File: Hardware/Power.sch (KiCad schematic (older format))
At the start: 20 parts, among them U8 AOZ1280

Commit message: Clear annotations
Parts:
- renumbered C39 to C?, C41 to C?, C44 to C?, D36 to D?, L2 to L?, R37 to R?, R38 to R?, R34 to R?, SH1 to SH?, SH2 to SH?, SH3 to SH?, SH4 to SH?, U8 to U?
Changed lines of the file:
@@
 $EndDescr
 $Comp
-L +3.3V #PWR099
+L +3.3V #PWR?
 U 1 1 5241F48B
 P 5300 4800
-F 0 "#PWR099" H 5300 4760 30  0001 C CNN
+F 0 "#PWR?" H 5300 4760 30  0001 C CNN
 F 1 "+3.3V" H 5300 4910 30  0000 C CNN
 F 2 "" H 5300 4800 60  0000 C CNN
@@
 $EndComp
 $Comp
-L AOZ1280 U8
+L AOZ1280 U?
 U 1 1 52455ED9
 P 3550 5250
-F 0 "U8" H 3550 4800 60  0000 C CNN
+F 0 "U?" H 3550 4800 60  0000 C CNN
 F 1 "AOZ1280" V 3550 5250 60  0000 C CNN
 F 2 "" H 3550 5600 60  0000 C CNN
@@
 $EndComp
 $Comp
-L DIODE-SCH D36
+L DIODE-SCH D?
 U 1 1 52455EF2
 P 4100 5250
-F 0 "D36" H 4100 5350 60  0000 C CNN
+F 0 "D?" H 4100 5350 60  0000 C CNN
 F 1 "CDBA140" H 4100 5150 60  0000 C CNN
 F 2 "~" H 4100 5250 60  0000 C CNN
@@
 $EndComp
 $Comp
-L R R37
+L R R?
 U 1 1 52455F0B
 P 4800 5250
-F 0 "R37" H 4800 5350 50  0000 C CNN
+F 0 "R?" H 4800 5350 50  0000 C CNN
 F 1 "49.9k" H 4800 5250 50  0000 C CNN
 F 2 "RESC1608" H 4800 5250 60  0001 C CNN
@@
 $EndComp
 $Comp
-L R R38
+L R R?
 U 1 1 52455F41
 P 4800 5950
-F 0 "R38" H 4800 6050 50  0000 C CNN
+F 0 "R?" H 4800 6050 50  0000 C CNN
 F 1 "15.8k" H 4800 5950 50  0000 C CNN
 F 2 "RESC1608" H 4800 5950 60  0001 C CNN
@@
 $EndComp
 $Comp
-L GND #PWR0106
+L GND #PWR?
 U 1 1 5245631B
 P 2400 5800
-F 0 "#PWR0106" H 2400 5800 30  0001 C CNN
+F 0 "#PWR?" H 2400 5800 30  0001 C CNN
 F 1 "GND" H 2400 5730 30  0001 C CNN
 F 2 "" H 2400 5800 60  0000 C CNN
@@
 $EndComp
 $Comp
-L GND #PWR0107
+L GND #PWR?
 U 1 1 5245632A
 P 3000 5700
-F 0 "#PWR0107" H 3000 5700 30  0001 C CNN
+F 0 "#PWR?" H 3000 5700 30  0001 C CNN
 F 1 "GND" H 3000 5630 30  0001 C CNN
 F 2 "" H 3000 5700 60  0000 C CNN
@@
 $EndComp
 $Comp
-L GND #PWR0108
+L GND #PWR?
 U 1 1 52456339
 P 5300 5600
-F 0 "#PWR0108" H 5300 5600 30  0001 C CNN
+F 0 "#PWR?" H 5300 5600 30  0001 C CNN
 F 1 "GND" H 5300 5530 30  0001 C CNN
 F 2 "" H 5300 5600 60  0000 C CNN
@@
 $EndComp
 $Comp
-L GND #PWR0109
+L GND #PWR?
 U 1 1 52456348
 P 4800 6300
-F 0 "#PWR0109" H 4800 6300 30  0001 C CNN
+F 0 "#PWR?" H 4800 6300 30  0001 C CNN
 F 1 "GND" H 4800 6230 30  0001 C CNN
 F 2 "" H 4800 6300 60  0000 C CNN
@@
 $EndComp
 $Comp
-L GND #PWR0110
+L GND #PWR?
 U 1 1 52456357
 P 4100 5700
-F 0 "#PWR0110" H 4100 5700 30  0001 C CNN
+F 0 "#PWR?" H 4100 5700 30  0001 C CNN
 F 1 "GND" H 4100 5630 30  0001 C CNN
 F 2 "" H 4100 5700 60  0000 C CNN
@@
 $EndComp
 $Comp
-L L L2
+L L L?
 U 1 1 524569D1
 P 4450 4900
-F 0 "L2" H 4450 4800 60  0000 C CNN
+F 0 "L?" H 4450 4800 60  0000 C CNN
 F 1 "10uH" H 4450 4950 60  0000 C CNN
 F 2 "INDC3225" H 4450 4900 60  0001 C CNN
@@
 $EndComp
 $Comp
-L C C39
+L C C?
 U 1 1 52456A9F
 P 2400 5450
-F 0 "C39" H 2450 5600 60  0000 L CNN
+F 0 "C?" H 2450 5600 60  0000 L CNN
 F 1 "10uF" H 2450 5300 60  0000 L CNN
 F 2 "~" H 2400 5450 60  0000 C CNN
@@
 Lx
 $Comp
-L C C41
+L C C?
 U 1 1 52457190
 P 3550 4500
-F 0 "C41" H 3600 4650 60  0000 L CNN
+F 0 "C?" H 3600 4650 60  0000 L CNN
 F 1 "0.01uF" H 3600 4350 60  0000 L CNN
 F 2 "CAPC1608" H 3550 4500 60  0001 C CNN
@@
 $EndComp
 $Comp
-L C C44
+L C C?
 U 1 1 5245816D
 P 5300 5250
-F 0 "C44" H 5350 5400 60  0000 L CNN
+F 0 "C?" H 5350 5400 60  0000 L CNN
 F 1 "10uF" H 5350 5100 60  0000 L CNN
 F 2 "~" H 5300 5250 60  0000 C CNN
@@
 Bst
 $Comp
-L TP SH1
+L TP SH?
 U 1 1 52BCE4A7
 P 7600 3400
-F 0 "SH1" H 7600 3750 60  0000 C CNN
+F 0 "SH?" H 7600 3750 60  0000 C CNN
 F 1 "SHIELD" H 7600 3650 60  0000 C CNN
 F 2 "EMI-TE-155157X" H 7600 3400 60  0001 C CNN
@@
 $EndComp
 $Comp
-L TP SH2
+L TP SH?
 U 1 1 52BCE50F
 P 8000 3400
-F 0 "SH2" H 8000 3750 60  0000 C CNN
+F 0 "SH?" H 8000 3750 60  0000 C CNN
 F 1 "SHIELD" H 8000 3650 60  0000 C CNN
 F 2 "EMI-TE-155157X" H 8000 3400 60  0001 C CNN
@@
 $EndComp
 $Comp
-L TP SH3
+L TP SH?
 U 1 1 52BCE518
 P 8400 3400
-F 0 "SH3" H 8400 3750 60  0000 C CNN
+F 0 "SH?" H 8400 3750 60  0000 C CNN
 F 1 "SHIELD" H 8400 3650 60  0000 C CNN
 F 2 "EMI-TE-155157X" H 8400 3400 60  0001 C CNN
@@
 $EndComp
 $Comp
-L TP SH4
+L TP SH?
 U 1 1 52BCE521
 P 8800 3400
-F 0 "SH4" H 8800 3750 60  0000 C CNN
+F 0 "SH?" H 8800 3750 60  0000 C CNN
 F 1 "SHIELD" H 8800 3650 60  0000 C CNN
 F 2 "EMI-TE-155157X" H 8800 3400 60  0001 C CNN
@@
 $EndComp
 $Comp
-L GND #PWR0111
+L GND #PWR?
 U 1 1 52BCE529
 P 8200 3600
-F 0 "#PWR0111" H 8200 3600 30  0001 C CNN
+F 0 "#PWR?" H 8200 3600 30  0001 C CNN
 F 1 "GND" H 8200 3530 30  0001 C CNN
 F 2 "" H 8200 3600 60  0000 C CNN
@@
 $EndComp
 $Comp
-L R R34
+L R R?
 U 1 1 5411D30B
 P 2750 5100
-F 0 "R34" H 2750 5200 50  0000 C CNN
+F 0 "R?" H 2750 5200 50  0000 C CNN
 F 1 "10k" H 2750 5100 50  0000 C CNN
 F 2 "RESC1608" H 2750 5100 60  0001 C CNN
@@
 $EndComp
 $Comp
-L PWR_FLAG #FLG0112
+L PWR_FLAG #FLG?
 U 1 1 54122098
 P 4800 4800
-F 0 "#FLG0112" H 4800 4895 30  0001 C CNN
+F 0 "#FLG?" H 4800 4895 30  0001 C CNN
 F 1 "PWR_FLAG" H 4800 4980 30  0000 C CNN
 F 2 "" H 4800 4800 60  0000 C CNN

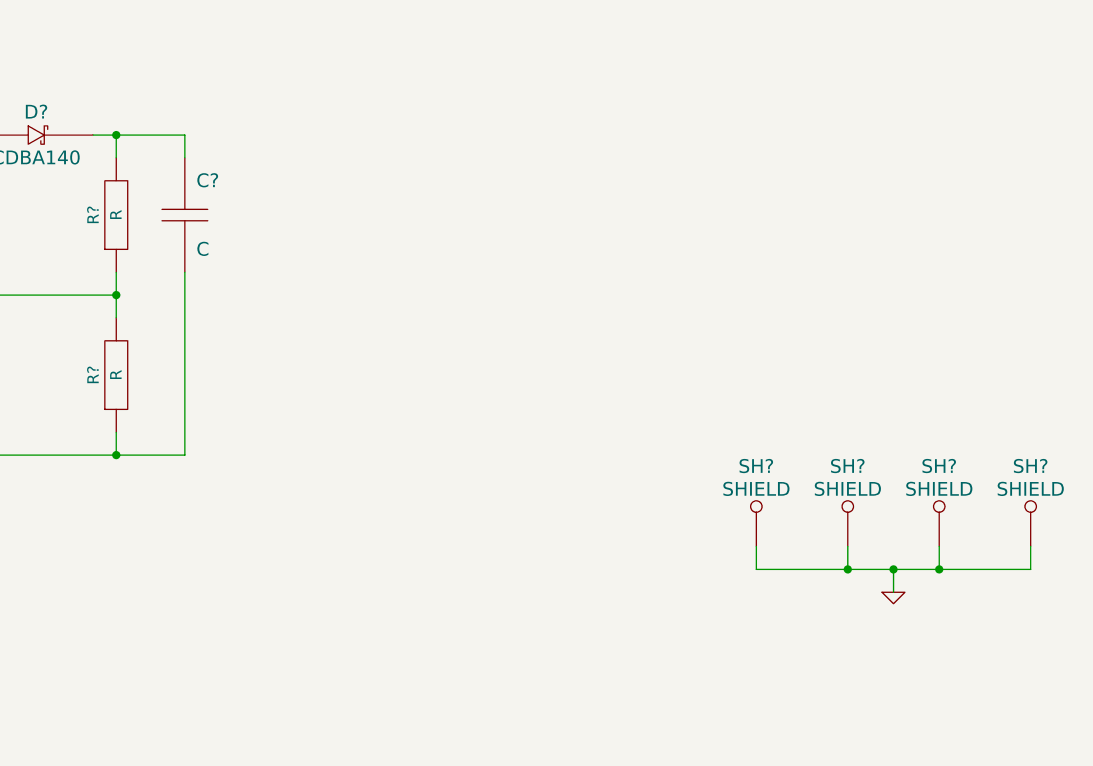
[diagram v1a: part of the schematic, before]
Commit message: Add LDO for analog
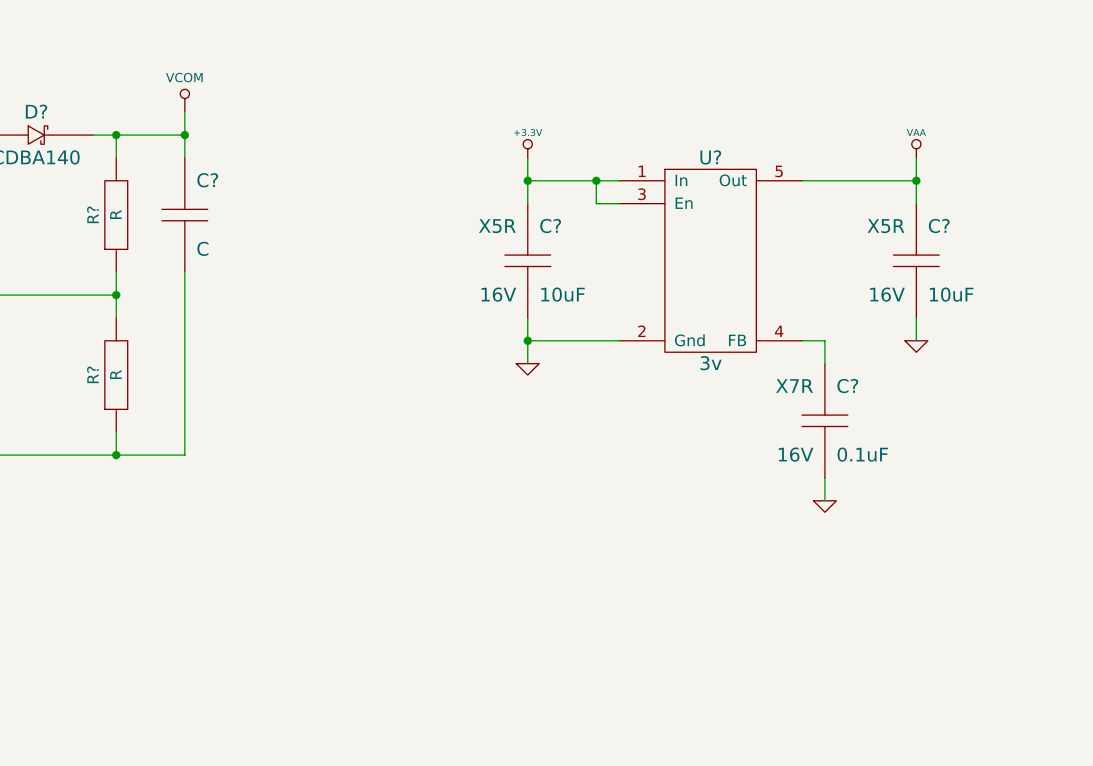
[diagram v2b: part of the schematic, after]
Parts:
- removed SH? (x4): SHIELD, EMI-TE-155157X, symbol TP
- added C?: 0.1uF, CAPC1608, symbol C
- added C? (x2): 10uF, ~, symbol C
- added U?: 3v, symbol LDO-5
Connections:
- net +3.3V: now also C?.1, U?.1 (In), U?.3 (En)
- net GND: now also C?.2, C?.2, C?.2, U?.2 (Gnd)
- net VCOM: now reaches C?.1, D?.2, R?.2
- new net: C?.1, U?.4 (FB)
- new net VAA: C?.1, U?.5 (Out)
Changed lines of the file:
@@
 Sheet 5 5
 Title ""
-Date "22 sep 2014"
+Date "23 sep 2014"
 Rev ""
 Comp ""
@@
 Bst
 $Comp
-L TP SH?
-U 1 1 52BCE4A7
-P 7600 3400
-F 0 "SH?" H 7600 3750 60  0000 C CNN
-F 1 "SHIELD" H 7600 3650 60  0000 C CNN
-F 2 "EMI-TE-155157X" H 7600 3400 60  0001 C CNN
-F 3 "~" H 7600 3400 60  0000 C CNN
-F 4 "TE" H 7600 3400 60  0001 C CNN "MFR Name"
-F 5 "1551573-5" H 7600 3400 60  0001 C CNN "MFR Part No"
-F 6 "A104054CT-ND" H 7600 3400 60  0001 C CNN "Distributor Part No"
-	1    7600 3400
-	1    0    0    -1
-$EndComp
-$Comp
-L TP SH?
-U 1 1 52BCE50F
-P 8000 3400
-F 0 "SH?" H 8000 3750 60  0000 C CNN
-F 1 "SHIELD" H 8000 3650 60  0000 C CNN
-F 2 "EMI-TE-155157X" H 8000 3400 60  0001 C CNN
-F 3 "~" H 8000 3400 60  0000 C CNN
-F 4 "TE" H 8000 3400 60  0001 C CNN "MFR Name"
-F 5 "1551573-5" H 8000 3400 60  0001 C CNN "MFR Part No"
-F 6 "A104054CT-ND" H 8000 3400 60  0001 C CNN "Distributor Part No"
-	1    8000 3400
-	1    0    0    -1
-$EndComp
-$Comp
-L TP SH?
-U 1 1 52BCE518
-P 8400 3400
-F 0 "SH?" H 8400 3750 60  0000 C CNN
-F 1 "SHIELD" H 8400 3650 60  0000 C CNN
-F 2 "EMI-TE-155157X" H 8400 3400 60  0001 C CNN
-F 3 "~" H 8400 3400 60  0000 C CNN
-F 4 "TE" H 8400 3400 60  0001 C CNN "MFR Name"
-F 5 "1551573-5" H 8400 3400 60  0001 C CNN "MFR Part No"
-F 6 "A104054CT-ND" H 8400 3400 60  0001 C CNN "Distributor Part No"
-	1    8400 3400
-	1    0    0    -1
-$EndComp
-$Comp
-L TP SH?
-U 1 1 52BCE521
-P 8800 3400
-F 0 "SH?" H 8800 3750 60  0000 C CNN
-F 1 "SHIELD" H 8800 3650 60  0000 C CNN
-F 2 "EMI-TE-155157X" H 8800 3400 60  0001 C CNN
-F 3 "~" H 8800 3400 60  0000 C CNN
-F 4 "TE" H 8800 3400 60  0001 C CNN "MFR Name"
-F 5 "1551573-5" H 8800 3400 60  0001 C CNN "MFR Part No"
-F 6 "A104054CT-ND" H 8800 3400 60  0001 C CNN "Distributor Part No"
-	1    8800 3400
-	1    0    0    -1
-$EndComp
-$Comp
-L GND #PWR?
-U 1 1 52BCE529
-P 8200 3600
-F 0 "#PWR?" H 8200 3600 30  0001 C CNN
-F 1 "GND" H 8200 3530 30  0001 C CNN
-F 2 "" H 8200 3600 60  0000 C CNN
-F 3 "" H 8200 3600 60  0000 C CNN
-	1    8200 3600
-	1    0    0    -1
-$EndComp
-$Comp
 L R R?
 U 1 1 5411D30B
@@
 Connection ~ 3000 4500
 Wire Wire Line
-	7600 3400 7600 3500
-Wire Wire Line
-	7600 3500 8800 3500
-Wire Wire Line
-	8800 3500 8800 3400
-Wire Wire Line
-	8400 3400 8400 3500
-Connection ~ 8400 3500
-Wire Wire Line
-	8000 3400 8000 3500
-Connection ~ 8000 3500
-Wire Wire Line
-	8200 3600 8200 3500
-Connection ~ 8200 3500
-Wire Wire Line
 	3850 1200 4100 1200
 Wire Wire Line
@@
 	4700 1600 5100 1600
 Wire Wire Line
-	5100 1600 5100 1700
+	5100 1500 5100 1700
 Wire Wire Line
 	4800 1700 4800 1600
@@
 	1    0    0    -1
 $EndComp
+$Comp
+L VCOM #PWR?
+U 1 1 5421D060
+P 5100 1500
+F 0 "#PWR?" H 5100 1700 40  0001 C CNN
+F 1 "VCOM" H 5100 1650 40  0000 C CNN
+F 2 "" H 5100 1500 60  0000 C CNN
+F 3 "" H 5100 1500 60  0000 C CNN
+	1    5100 1500
+	1    0    0    -1
+$EndComp
+Connection ~ 5100 1600
+$Comp
+L LDO-5 U?
+U 1 1 5421D8A9
+P 7400 2150
+F 0 "U?" H 7400 2600 60  0000 C CNN
+F 1 "3v" H 7400 1700 60  0000 C CNN
+F 2 "" H 7400 2150 60  0000 C CNN
+F 3 "" H 7400 2150 60  0000 C CNN
+F 4 "TI" H 7400 2150 60  0001 C CNN "MFR Name"
+F 5 "TPS73130DBVT" H 7400 2150 60  0001 C CNN "MFR Part No"
+F 6 "296-15804-1-ND" H 7400 2150 60  0001 C CNN "Distributor Part No"
+	1    7400 2150
+	1    0    0    -1
+$EndComp
+$Comp
+L C C?
+U 1 1 5421D92A
+P 7900 2850
+F 0 "C?" H 7950 3000 60  0000 L CNN
+F 1 "0.1uF" H 7950 2700 60  0000 L CNN
+F 2 "CAPC1608" H 7900 2850 60  0001 C CNN
+F 3 "~" H 7900 2850 60  0000 C CNN
+F 4 "Samsung" H 7900 2850 60  0001 C CNN "MFR Name"
+F 5 "CL10B104KO8NNNC" H 7900 2850 60  0001 C CNN "MFR Part No"
+F 6 "1276-1005-1-ND" H 7900 2850 60  0001 C CNN "Distributor Part No"
+F 7 "16V" H 7850 2700 60  0000 R CNN "Voltage"
+F 8 "X7R" H 7850 3000 60  0000 R CNN "Dielectric"
+	1    7900 2850
+	1    0    0    -1
+$EndComp
+$Comp
+L C C?
+U 1 1 5421D961
+P 8300 2150
+F 0 "C?" H 8350 2300 60  0000 L CNN
+F 1 "10uF" H 8350 2000 60  0000 L CNN
+F 2 "~" H 8300 2150 60  0000 C CNN
+F 3 "~" H 8300 2150 60  0000 C CNN
+F 4 "Taiyo Yuden" H 8300 2150 60  0001 C CNN "MFR Name"
+F 5 "EMK212BJ106KG-T" H 8300 2150 60  0001 C CNN "MFR Part No"
+F 6 "587-1295-1-ND" H 8300 2150 60  0001 C CNN "Distributor Part No"
+F 7 "16V" H 8250 2000 60  0000 R CNN "Voltage"
+F 8 "X5R" H 8250 2300 60  0000 R CNN "Dielectric"
+	1    8300 2150
+	1    0    0    -1
+$EndComp
+$Comp
+L C C?
+U 1 1 5421D96C
+P 6600 2150
+F 0 "C?" H 6650 2300 60  0000 L CNN
+F 1 "10uF" H 6650 2000 60  0000 L CNN
+F 2 "~" H 6600 2150 60  0000 C CNN
+F 3 "~" H 6600 2150 60  0000 C CNN
+F 4 "Taiyo Yuden" H 6600 2150 60  0001 C CNN "MFR Name"
+F 5 "EMK212BJ106KG-T" H 6600 2150 60  0001 C CNN "MFR Part No"
+F 6 "587-1295-1-ND" H 6600 2150 60  0001 C CNN "Distributor Part No"
+F 7 "16V" H 6550 2000 60  0000 R CNN "Voltage"
+F 8 "X5R" H 6550 2300 60  0000 R CNN "Dielectric"
+	1    6600 2150
+	1    0    0    -1
+$EndComp
+$Comp
+L +3.3V #PWR?
+U 1 1 5421D974
+P 6600 1700
+F 0 "#PWR?" H 6600 1660 30  0001 C CNN
+F 1 "+3.3V" H 6600 1810 30  0000 C CNN
+F 2 "" H 6600 1700 60  0000 C CNN
+F 3 "" H 6600 1700 60  0000 C CNN
+	1    6600 1700
+	1    0    0    -1
+$EndComp
+Wire Wire Line
+	6600 1700 6600 1900
+Wire Wire Line
+	7000 1800 6600 1800
+Connection ~ 6600 1800
+Wire Wire Line
+	7000 1900 6900 1900
+Wire Wire Line
+	6900 1900 6900 1800
+Connection ~ 6900 1800
+$Comp
+L GND #PWR?
+U 1 1 5421DA38
+P 6600 2600
+F 0 "#PWR?" H 6600 2600 30  0001 C CNN
+F 1 "GND" H 6600 2530 30  0001 C CNN
+F 2 "" H 6600 2600 60  0000 C CNN
+F 3 "" H 6600 2600 60  0000 C CNN
+	1    6600 2600
+	1    0    0    -1
+$EndComp
+Wire Wire Line
+	6600 2400 6600 2600
+Wire Wire Line
+	7000 2500 6600 2500
+Connection ~ 6600 2500
+$Comp
+L GND #PWR?
+U 1 1 5421DACA
+P 7900 3200
+F 0 "#PWR?" H 7900 3200 30  0001 C CNN
+F 1 "GND" H 7900 3130 30  0001 C CNN
+F 2 "" H 7900 3200 60  0000 C CNN
+F 3 "" H 7900 3200 60  0000 C CNN
+	1    7900 3200
+	1    0    0    -1
+$EndComp
+$Comp
+L GND #PWR?
+U 1 1 5421DAD9
+P 8300 2500
+F 0 "#PWR?" H 8300 2500 30  0001 C CNN
+F 1 "GND" H 8300 2430 30  0001 C CNN
+F 2 "" H 8300 2500 60  0000 C CNN
+F 3 "" H 8300 2500 60  0000 C CNN
+	1    8300 2500
+	1    0    0    -1
+$EndComp
+Wire Wire Line
+	8300 2500 8300 2400
+Wire Wire Line
+	7900 3100 7900 3200
+$Comp
+L VAA #PWR?
+U 1 1 5421DB71
+P 8300 1700
+F 0 "#PWR?" H 8300 1760 30  0001 C CNN
+F 1 "VAA" H 8300 1810 30  0000 C CNN
+F 2 "" H 8300 1700 60  0000 C CNN
+F 3 "" H 8300 1700 60  0000 C CNN
+	1    8300 1700
+	1    0    0    -1
+$EndComp
+Wire Wire Line
+	8300 1700 8300 1900
+Wire Wire Line
+	7800 1800 8300 1800
+Connection ~ 8300 1800
+Wire Wire Line
+	7800 2500 7900 2500
+Wire Wire Line
+	7900 2500 7900 2600
 $EndSCHEMATC

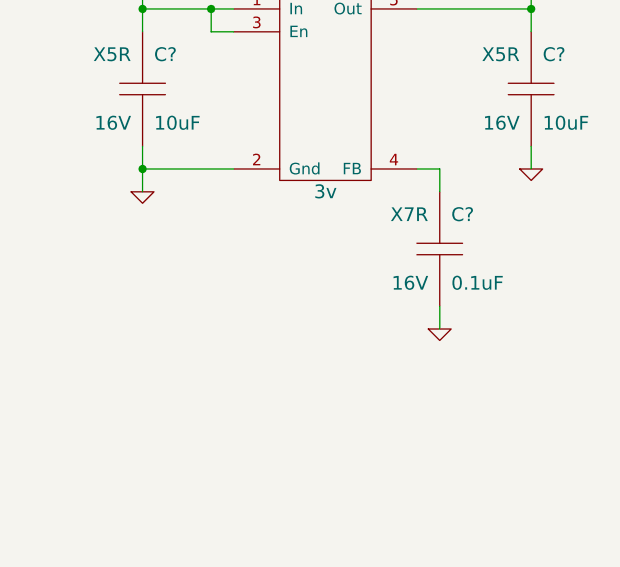
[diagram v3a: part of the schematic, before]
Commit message: Component values
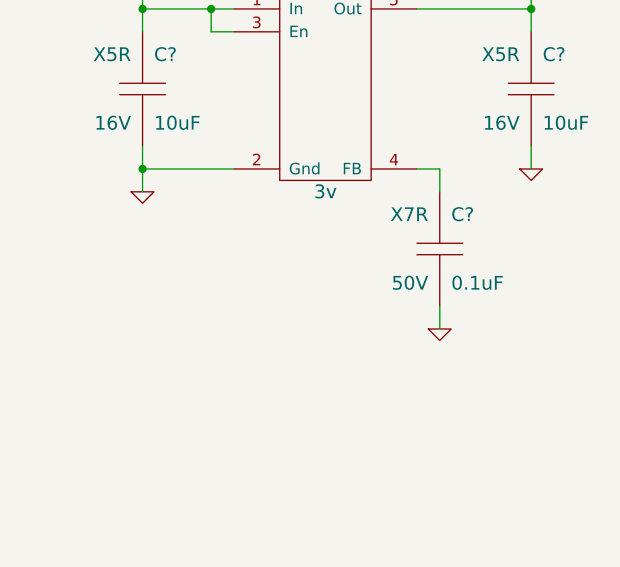
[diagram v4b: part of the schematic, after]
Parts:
- removed C?: 0.1uF, CAPC1608, symbol C
- added C?: 0.1uF, CAPC1608, symbol C
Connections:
- net GND: now also C?.2
- net at U?.4 (FB): now also C?.1
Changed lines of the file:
@@
 Sheet 5 5
 Title ""
-Date "23 sep 2014"
+Date "24 sep 2014"
 Rev ""
 Comp ""
@@
 $EndDescr
 $Comp
-L +3.3V #PWR061
+L +3.3V #PWR?
 U 1 1 5241F48B
 P 5300 4800
-F 0 "#PWR061" H 5300 4760 30  0001 C CNN
+F 0 "#PWR?" H 5300 4760 30  0001 C CNN
 F 1 "+3.3V" H 5300 4910 30  0000 C CNN
 F 2 "" H 5300 4800 60  0000 C CNN
@@
 $EndComp
 $Comp
-L GND #PWR062
+L GND #PWR?
 U 1 1 5245631B
 P 2400 5800
-F 0 "#PWR062" H 2400 5800 30  0001 C CNN
+F 0 "#PWR?" H 2400 5800 30  0001 C CNN
 F 1 "GND" H 2400 5730 30  0001 C CNN
 F 2 "" H 2400 5800 60  0000 C CNN
@@
 $EndComp
 $Comp
-L GND #PWR063
+L GND #PWR?
 U 1 1 5245632A
 P 3000 5700
-F 0 "#PWR063" H 3000 5700 30  0001 C CNN
+F 0 "#PWR?" H 3000 5700 30  0001 C CNN
 F 1 "GND" H 3000 5630 30  0001 C CNN
 F 2 "" H 3000 5700 60  0000 C CNN
@@
 $EndComp
 $Comp
-L GND #PWR064
+L GND #PWR?
 U 1 1 52456339
 P 5300 5600
-F 0 "#PWR064" H 5300 5600 30  0001 C CNN
+F 0 "#PWR?" H 5300 5600 30  0001 C CNN
 F 1 "GND" H 5300 5530 30  0001 C CNN
 F 2 "" H 5300 5600 60  0000 C CNN
@@
 $EndComp
 $Comp
-L GND #PWR065
+L GND #PWR?
 U 1 1 52456348
 P 4800 6300
-F 0 "#PWR065" H 4800 6300 30  0001 C CNN
+F 0 "#PWR?" H 4800 6300 30  0001 C CNN
 F 1 "GND" H 4800 6230 30  0001 C CNN
 F 2 "" H 4800 6300 60  0000 C CNN
@@
 $EndComp
 $Comp
-L GND #PWR066
+L GND #PWR?
 U 1 1 52456357
 P 4100 5700
-F 0 "#PWR066" H 4100 5700 30  0001 C CNN
+F 0 "#PWR?" H 4100 5700 30  0001 C CNN
 F 1 "GND" H 4100 5630 30  0001 C CNN
 F 2 "" H 4100 5700 60  0000 C CNN
@@
 $EndComp
 $Comp
-L PWR_FLAG #FLG067
+L PWR_FLAG #FLG?
 U 1 1 54122098
 P 4800 4800
-F 0 "#FLG067" H 4800 4895 30  0001 C CNN
+F 0 "#FLG?" H 4800 4895 30  0001 C CNN
 F 1 "PWR_FLAG" H 4800 4980 30  0000 C CNN
 F 2 "" H 4800 4800 60  0000 C CNN
@@
 Connection ~ 4800 2300
 $Comp
-L GND #PWR068
+L GND #PWR?
 U 1 1 54209E80
 P 3100 3100
-F 0 "#PWR068" H 3100 3100 30  0001 C CNN
+F 0 "#PWR?" H 3100 3100 30  0001 C CNN
 F 1 "GND" H 3100 3030 30  0001 C CNN
 F 2 "" H 3100 3100 60  0000 C CNN
@@
 	2900 1500 2900 1700
 $Comp
-L +BATT #PWR069
+L +BATT #PWR?
 U 1 1 54209FFB
 P 2900 1500
-F 0 "#PWR069" H 2900 1450 20  0001 C CNN
+F 0 "#PWR?" H 2900 1450 20  0001 C CNN
 F 1 "+BATT" H 2900 1600 30  0000 C CNN
 F 2 "" H 2900 1500 60  0000 C CNN
@@
 Connection ~ 2900 1600
 $Comp
-L +BATT #PWR070
+L +BATT #PWR?
 U 1 1 5420A04C
 P 2400 4800
-F 0 "#PWR070" H 2400 4750 20  0001 C CNN
+F 0 "#PWR?" H 2400 4750 20  0001 C CNN
 F 1 "+BATT" H 2400 4900 30  0000 C CNN
 F 2 "" H 2400 4800 60  0000 C CNN
@@
 F 6 "296-15804-1-ND" H 7400 2150 60  0001 C CNN "Distributor Part No"
 	1    7400 2150
-	1    0    0    -1
-$EndComp
-$Comp
-L C C?
-U 1 1 5421D92A
-P 7900 2850
-F 0 "C?" H 7950 3000 60  0000 L CNN
-F 1 "0.1uF" H 7950 2700 60  0000 L CNN
-F 2 "CAPC1608" H 7900 2850 60  0001 C CNN
-F 3 "~" H 7900 2850 60  0000 C CNN
-F 4 "Samsung" H 7900 2850 60  0001 C CNN "MFR Name"
-F 5 "CL10B104KO8NNNC" H 7900 2850 60  0001 C CNN "MFR Part No"
-F 6 "1276-1005-1-ND" H 7900 2850 60  0001 C CNN "Distributor Part No"
-F 7 "16V" H 7850 2700 60  0000 R CNN "Voltage"
-F 8 "X7R" H 7850 3000 60  0000 R CNN "Dielectric"
-	1    7900 2850
 	1    0    0    -1
 $EndComp
@@
 $EndComp
 $Comp
-L +3.3V #PWR071
+L +3.3V #PWR?
 U 1 1 5421D974
 P 6600 1700
-F 0 "#PWR071" H 6600 1660 30  0001 C CNN
+F 0 "#PWR?" H 6600 1660 30  0001 C CNN
 F 1 "+3.3V" H 6600 1810 30  0000 C CNN
 F 2 "" H 6600 1700 60  0000 C CNN
@@
 Connection ~ 6900 1800
 $Comp
-L GND #PWR072
+L GND #PWR?
 U 1 1 5421DA38
 P 6600 2600
-F 0 "#PWR072" H 6600 2600 30  0001 C CNN
+F 0 "#PWR?" H 6600 2600 30  0001 C CNN
 F 1 "GND" H 6600 2530 30  0001 C CNN
 F 2 "" H 6600 2600 60  0000 C CNN
@@
 Connection ~ 6600 2500
 $Comp
-L GND #PWR073
+L GND #PWR?
 U 1 1 5421DACA
 P 7900 3200
-F 0 "#PWR073" H 7900 3200 30  0001 C CNN
+F 0 "#PWR?" H 7900 3200 30  0001 C CNN
 F 1 "GND" H 7900 3130 30  0001 C CNN
 F 2 "" H 7900 3200 60  0000 C CNN
@@
 $EndComp
 $Comp
-L GND #PWR074
+L GND #PWR?
 U 1 1 5421DAD9
 P 8300 2500
-F 0 "#PWR074" H 8300 2500 30  0001 C CNN
+F 0 "#PWR?" H 8300 2500 30  0001 C CNN
 F 1 "GND" H 8300 2430 30  0001 C CNN
 F 2 "" H 8300 2500 60  0000 C CNN
@@
 	7900 3100 7900 3200
 $Comp
-L VAA #PWR075
+L VAA #PWR?
 U 1 1 5421DB71
 P 8300 1700
-F 0 "#PWR075" H 8300 1760 30  0001 C CNN
+F 0 "#PWR?" H 8300 1760 30  0001 C CNN
 F 1 "VAA" H 8300 1810 30  0000 C CNN
 F 2 "" H 8300 1700 60  0000 C CNN
@@
 Wire Wire Line
 	7900 2500 7900 2600
+$Comp
+L C C?
+U 1 1 5422232F
+P 7900 2850
+F 0 "C?" H 7950 3000 60  0000 L CNN
+F 1 "0.1uF" H 7950 2700 60  0000 L CNN
+F 2 "CAPC1608" H 7900 2850 60  0001 C CNN
+F 3 "~" H 7900 2850 60  0000 C CNN
+F 4 "Samsung" H 7900 2850 60  0001 C CNN "MFR Name"
+F 5 "CL10B104KB8SFNC" H 7900 2850 60  0001 C CNN "MFR Part No"
+F 6 "1276-1936-1-ND" H 7900 2850 60  0001 C CNN "Distributor Part No"
+F 7 "50V" H 7850 2700 60  0000 R CNN "Voltage"
+F 8 "X7R" H 7850 3000 60  0000 R CNN "Dielectric"
+	1    7900 2850
+	1    0    0    -1
+$EndComp
 $EndSCHEMATC
